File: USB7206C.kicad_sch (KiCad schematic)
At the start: 38 parts, among them J1 USB_SPI_(Opt), SW1 RESET_HUB, U1 USB7206C/KDX, U2 MIC803-29D4VM3-TR, Y1 25MHz

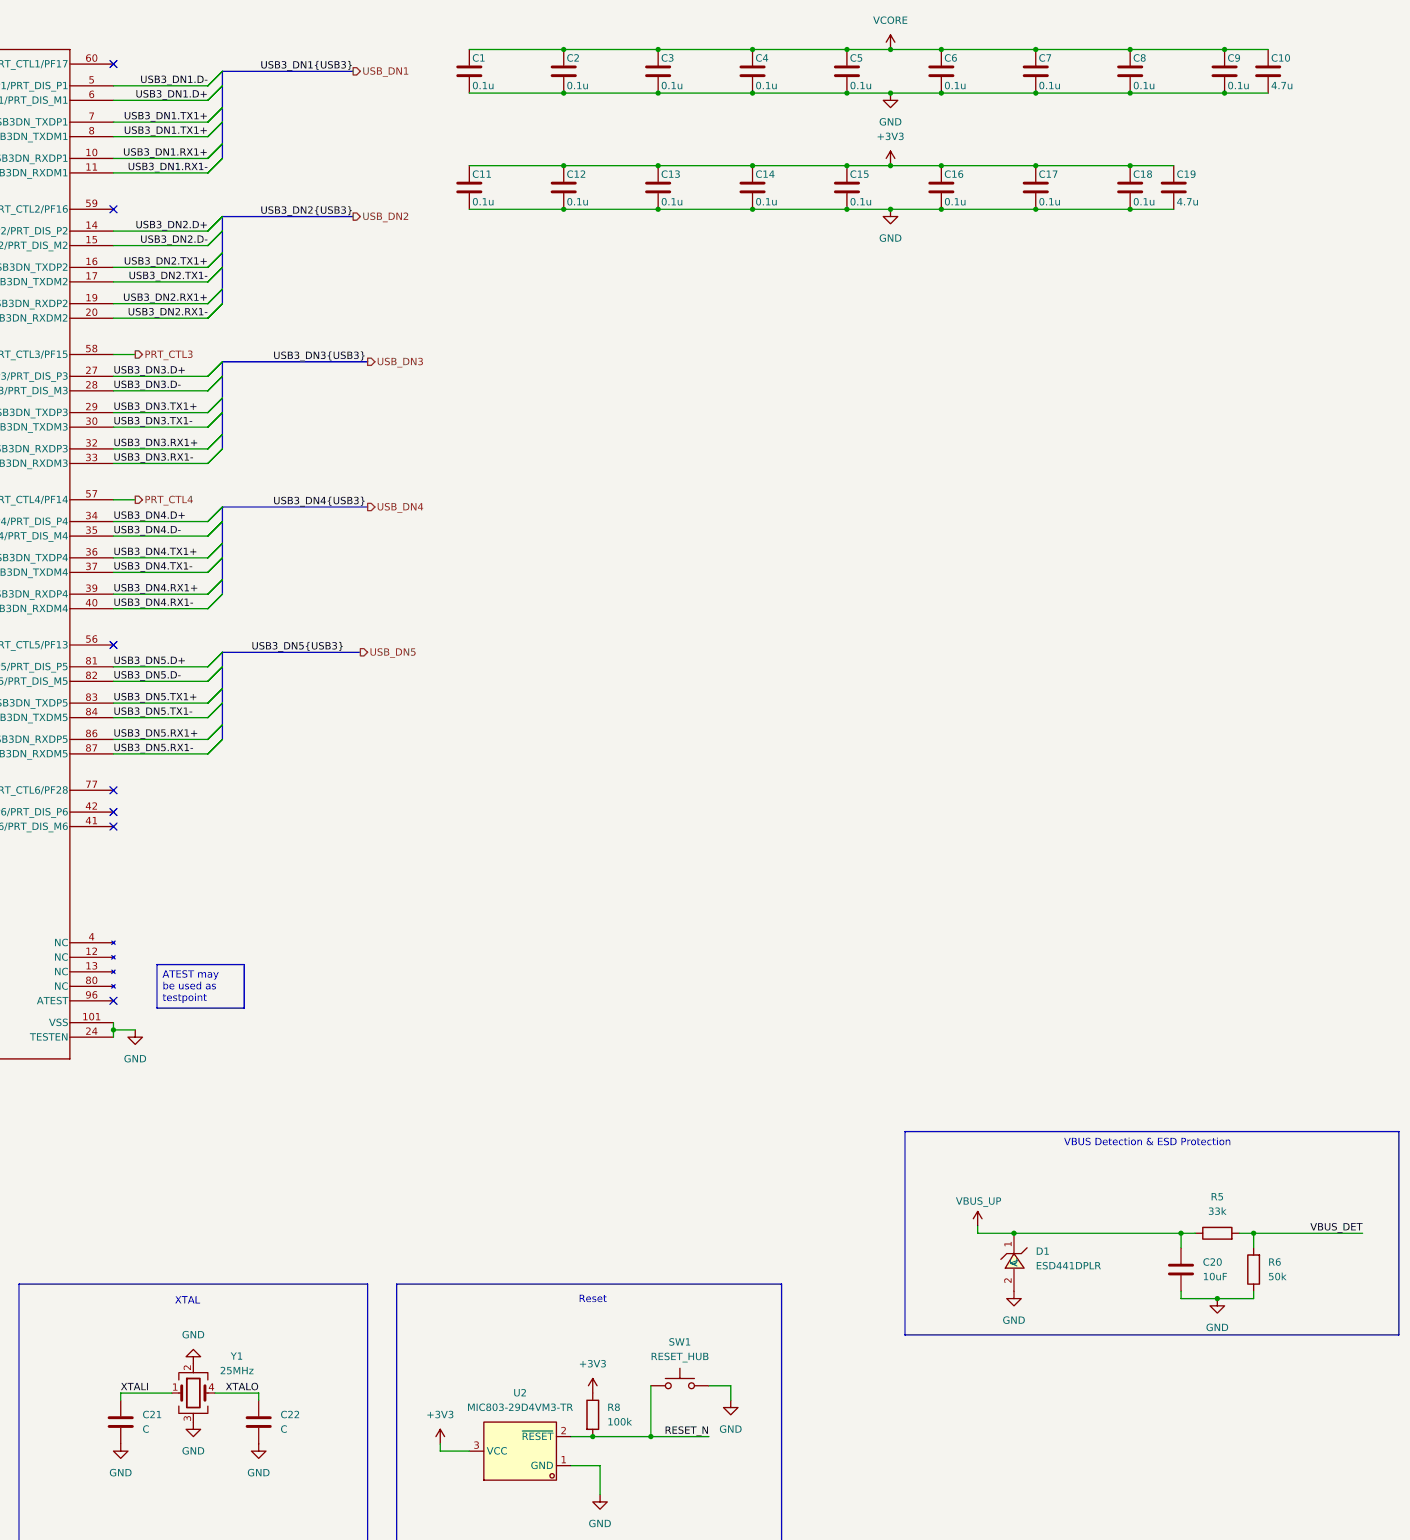
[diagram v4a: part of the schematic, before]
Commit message: Added lcsc part number for most of components, fixes for better routing
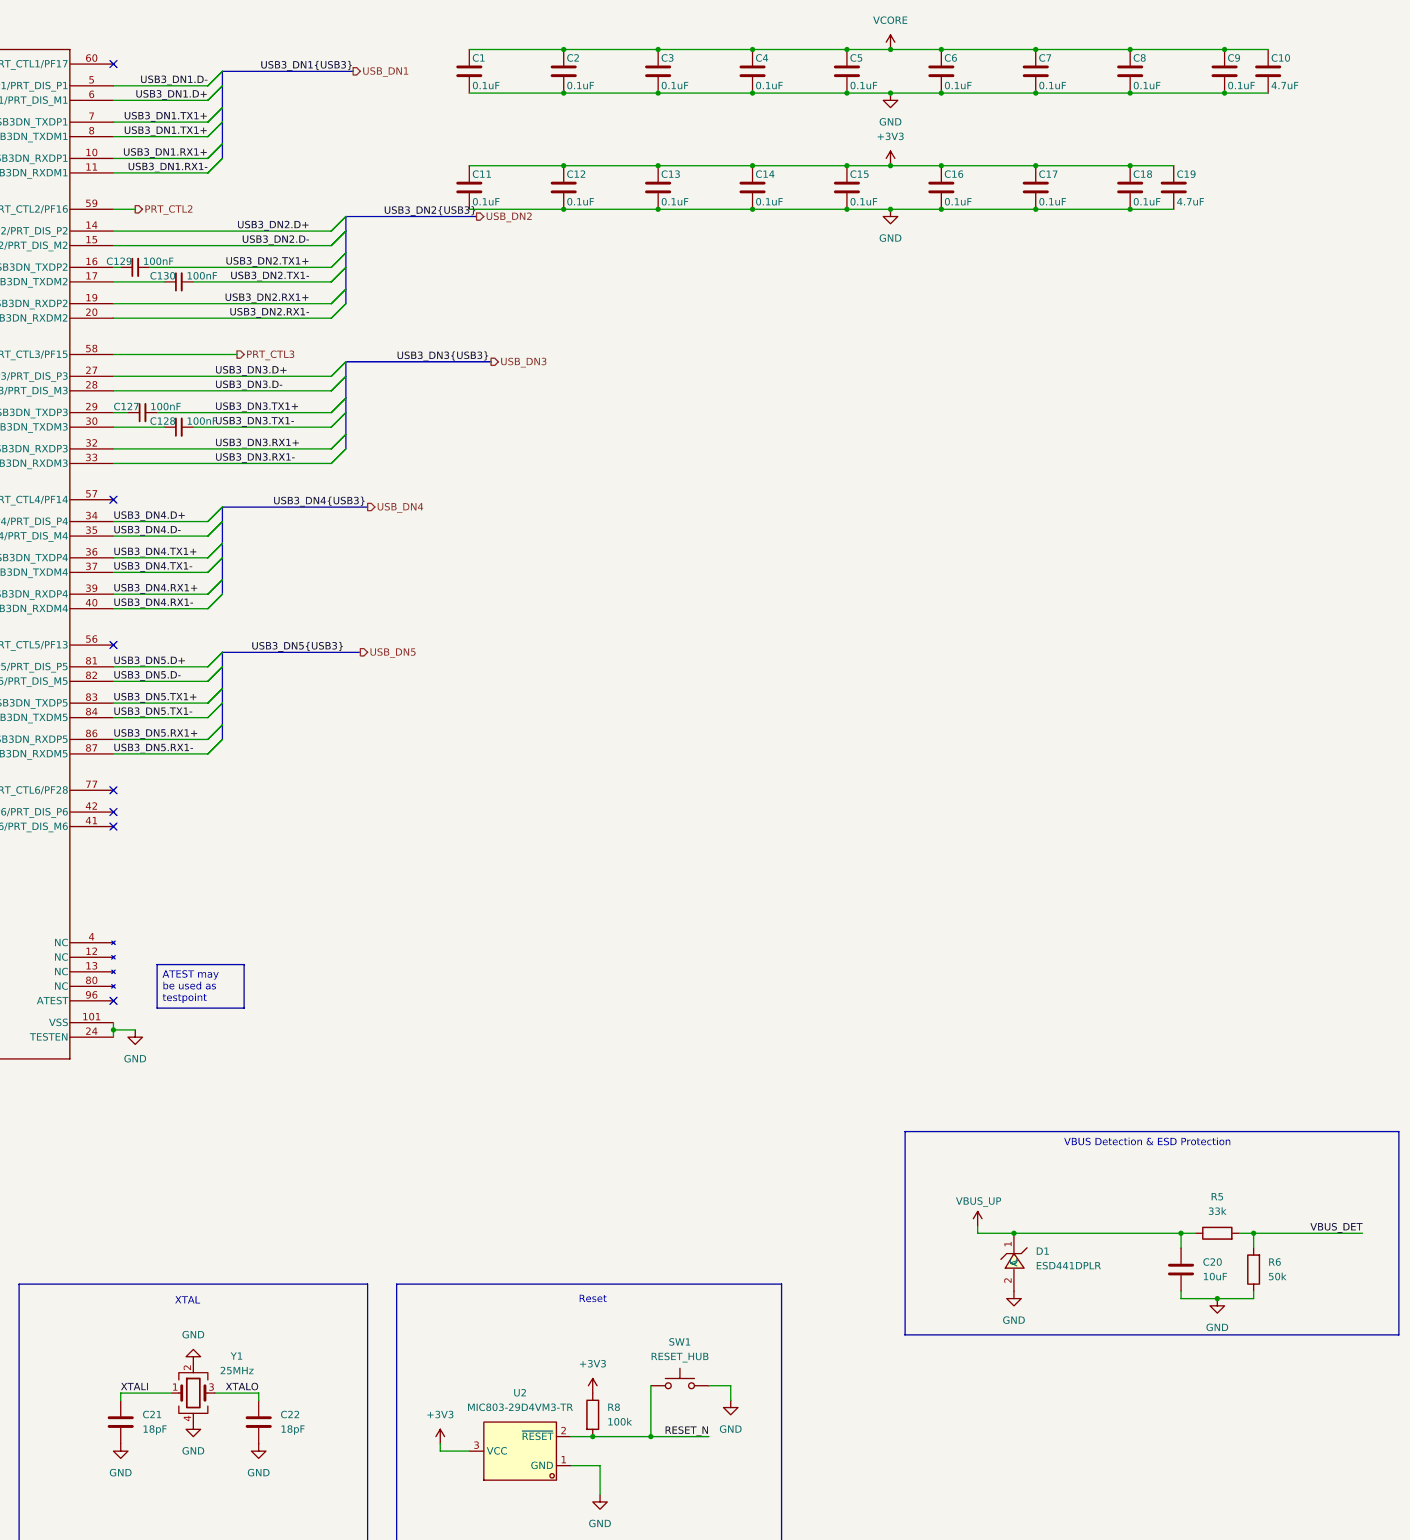
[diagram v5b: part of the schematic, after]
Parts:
- added C127, C128, C129, C130: 100nF, Capacitor_SMD:C_0402_1005Metric, symbol Device:C_Small
- C1, C11, C12, C13, C14, C15, C16, C17, C18, C2, C3, C4, C5, C6, C7, C8, C9: value 0.1u -> 0.1uF; LCSC Part (none) -> C5182432
- C10, C19: value 4.7u -> 4.7uF; footprint Capacitor_SMD:C_0402_1005Metric -> Capacitor_SMD:C_0805_2012Metric; LCSC Part (none) -> C6119944
- C20: footprint Capacitor_SMD:C_0402_1005Metric -> Capacitor_SMD:C_0805_2012Metric; LCSC Part (none) -> C3039694
- C21, C22: value C -> 18pF; LCSC Part (none) -> C33149
- Y1: footprint Crystal:Crystal_SMD_0603-4Pin_6.0x3.5mm -> Crystal:Crystal_SMD_3225-4Pin_3.2x2.5mm; LCSC Part (none) -> C179643
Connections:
- net GND: now also Y1.4; no longer Y1.3
- net USB3_DN2.TX1+: now also C129.2; no longer U1.16 (USB3DN_TXDP2)
- net USB3_DN2.TX1-: now also C130.2; no longer U1.17 (USB3DN_TXDM2)
- net USB3_DN3.TX1+: now also C127.2; no longer U1.29 (USB3DN_TXDP3)
- net USB3_DN3.TX1-: now also C128.2; no longer U1.30 (USB3DN_TXDM3)
- net XTALO: now also Y1.3; no longer Y1.4
- net PRT_CTL2: now reaches U1.59 (PRT_CTL2/PF16)
- net PRT_CTL4: no longer names the net of U1.57 (PRT_CTL4/PF14)
- new net: C130.1, U1.17 (USB3DN_TXDM2)
- new net: C127.1, U1.29 (USB3DN_TXDP3)
- new net: C128.1, U1.30 (USB3DN_TXDM3)
- new net: C129.1, U1.16 (USB3DN_TXDP2)

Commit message: Added lcsc part number for most of resistors
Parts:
- R1: LCSC Part (none) -> C102781
- R10, R9: LCSC Part (none) -> C25764
- R2, R3, R4, R7: LCSC Part (none) -> C25744
- R5: LCSC Part (none) -> C25779
- R6: LCSC Part (none) -> C166559
- R8: LCSC Part (none) -> C25741
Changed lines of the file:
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@@
 			)
 		)
+		(property "LCSC Part" "C25779 "
+			(at 365.76 227.33 90)
+			(effects
+				(font
+					(size 1.27 1.27)
+				)
+				(hide yes)
+			)
+		)
 		(pin "1"
 		)
@@
 			)
 		)
+		(property "LCSC Part" "C25741 "
+			(at 256.54 259.08 0)
+			(effects
+				(font
+					(size 1.27 1.27)
+				)
+				(hide yes)
+			)
+		)
 		(pin "2"
 		)
@@
 			)
 		)
+		(property "LCSC Part" "C25744"
+			(at 52.07 59.69 90)
+			(effects
+				(font
+					(size 1.27 1.27)
+				)
+				(hide yes)
+			)
+		)
 		(pin "1"
 		)
@@
 			)
 		)
+		(property "LCSC Part" "C25744"
+			(at 50.8 259.08 90)
+			(effects
+				(font
+					(size 1.27 1.27)
+				)
+				(hide yes)
+			)
+		)
 		(pin "2"
 		)
@@
 			)
 		)
+		(property "LCSC Part" "C25764 "
+			(at 50.8 264.16 90)
+			(effects
+				(font
+					(size 1.27 1.27)
+				)
+				(hide yes)
+			)
+		)
 		(pin "2"
 		)
@@
 			)
 		)
+		(property "LCSC Part" "C102781 "
+			(at 31.75 50.8 90)
+			(effects
+				(font
+					(size 1.27 1.27)
+				)
+				(hide yes)
+			)
+		)
 		(pin "1"
 		)
@@
 			)
 		)
+		(property "LCSC Part" "C25764 "
+			(at 50.8 261.62 90)
+			(effects
+				(font
+					(size 1.27 1.27)
+				)
+				(hide yes)
+			)
+		)
 		(pin "2"
 		)
@@
 			)
 		)
+		(property "LCSC Part" "C25744"
+			(at 52.07 54.61 90)
+			(effects
+				(font
+					(size 1.27 1.27)
+				)
+				(hide yes)
+			)
+		)
 		(pin "1"
 		)
@@
 			)
 		)
+		(property "LCSC Part" "C25744"
+			(at 52.07 57.15 90)
+			(effects
+				(font
+					(size 1.27 1.27)
+				)
+				(hide yes)
+			)
+		)
 		(pin "1"
 		)
@@
 			(at 372.11 233.68 0)
 			(effects
+				(font
+					(size 1.27 1.27)
+				)
+				(hide yes)
+			)
+		)
+		(property "LCSC Part" "C166559"
+			(at 372.11 233.68 0)
+			(effects

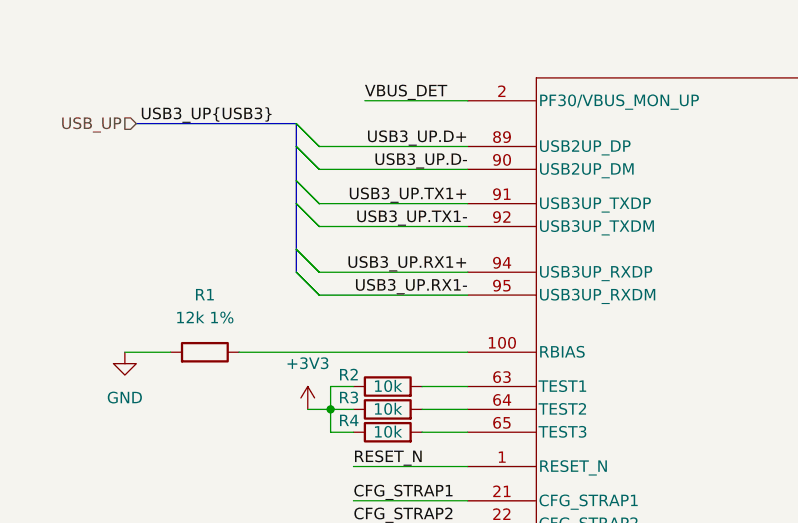
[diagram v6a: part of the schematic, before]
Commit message: minor schematic fixes, footprints changes, layout improvements
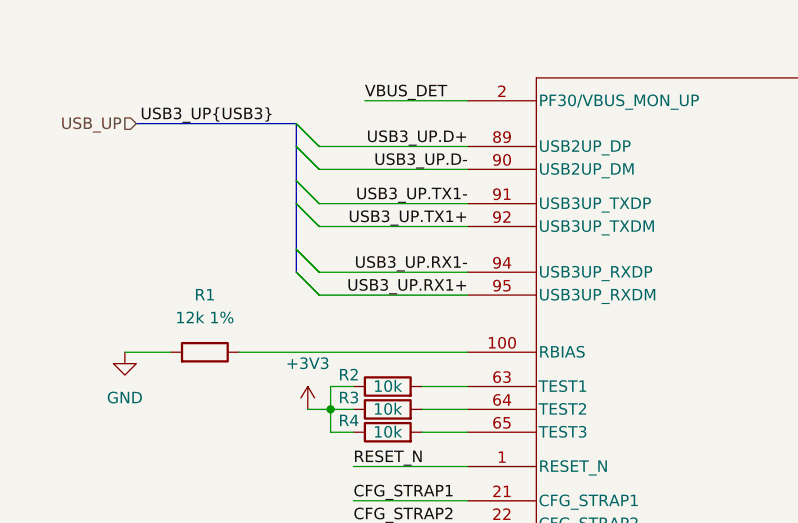
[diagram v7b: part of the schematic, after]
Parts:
- SW1: footprint Button_Switch_SMD:SW_Push_1P1T_XKB_TS-1187A -> EasyEDA:ultra_small_switch_1.6x3.0mm
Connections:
- net USB3_UP.RX1+: now also U1.95 (USB3UP_RXDM); no longer U1.94 (USB3UP_RXDP)
- net USB3_UP.RX1-: now also U1.94 (USB3UP_RXDP); no longer U1.95 (USB3UP_RXDM)
- net USB3_UP.TX1+: now also U1.92 (USB3UP_TXDM); no longer U1.91 (USB3UP_TXDP)
- net USB3_UP.TX1-: now also U1.91 (USB3UP_TXDP); no longer U1.92 (USB3UP_TXDM)
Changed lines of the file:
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@@
 		)
 	)
+	(wire
+		(pts
+			(xy 44.45 44.45) (xy 60.96 44.45)
+		)
+		(stroke
+			(width 0)
+			(type default)
+		)
+	)
 	(bus
 		(pts
@@
 	(wire
 		(pts
-			(xy 60.96 44.45) (xy 44.45 44.45)
-		)
-		(stroke
-			(width 0)
-			(type default)
-		)
-	)
-	(wire
-		(pts
 			(xy 186.69 60.96) (xy 210.82 60.96)
 		)
@@
 		)
 	)
-	(label "USB3_DN1.RX1+"
-		(at 189.23 39.37 180)
+	(label "USB3_UP.TX1-"
+		(at 60.96 34.29 180)
 		(effects
 			(font
@@
 		)
 	)
-	(label "USB3_UP.TX1+"
-		(at 60.96 34.29 180)
+	(label "USB3_DN1.RX1+"
+		(at 189.23 39.37 180)
 		(effects
 			(font
@@
 		)
 	)
+	(label "USB3_UP.TX1+"
+		(at 60.96 36.83 180)
+		(effects
+			(font
+				(size 1.27 1.27)
+			)
+			(justify right bottom)
+		)
+	)
 	(label "USB3_UP.D+"
 		(at 60.96 27.94 180)
@@
 		)
 	)
+	(label "USB3_UP.RX1-"
+		(at 60.96 41.91 180)
+		(effects
+			(font
+				(size 1.27 1.27)
+			)
+			(justify right bottom)
+		)
+	)
 	(label "USB3_DN2{USB3}"
 		(at 236.22 49.53 180)
@@
 		)
 	)
-	(label "USB3_UP.RX1-"
-		(at 60.96 44.45 180)
-		(effects
-			(font
-				(size 1.27 1.27)
-			)
-			(justify right bottom)
-		)
-	)
 	(label "USB3_DN1.D+"
 		(at 189.23 29.21 180)
@@
 		)
 	)
-	(label "USB3_UP.RX1+"
-		(at 60.96 41.91 180)
-		(effects
-			(font
-				(size 1.27 1.27)
-			)
-			(justify right bottom)
-		)
-	)
 	(label "USB3_DN1.D-"
 		(at 189.23 26.67 180)
@@
 		)
 	)
-	(label "USB3_UP.TX1-"
-		(at 60.96 36.83 180)
+	(label "USB3_DN3.D-"
+		(at 190.5 80.01 0)
 		(effects
 			(font
 				(size 1.27 1.27)
 			)
-			(justify right bottom)
+			(justify left bottom)
 		)
 	)
-	(label "USB3_DN3.D-"
-		(at 190.5 80.01 0)
+	(label "USB3_UP.RX1+"
+		(at 60.96 44.45 180)
 		(effects
 			(font
 				(size 1.27 1.27)
 			)
-			(justify left bottom)
+			(justify right bottom)
 		)
 	)
@@
 			)
 		)
-		(property "Footprint" "Button_Switch_SMD:SW_Push_1P1T_XKB_TS-1187A"
+		(property "Footprint" "EasyEDA:ultra_small_switch_1.6x3.0mm"
 			(at 271.78 248.92 0)
 			(effects

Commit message: comments to schematic added, changed a few components
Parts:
- SW1: LCSC Part (none) -> C913788
- U1: Mouser Part No  (none) -> 579-USB7206C/KDX
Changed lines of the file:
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@@
+			)
+		)
+		(property "LCSC Part" "C913788 "
+			(at 271.78 254 0)
+			(effects
+				(font
+					(size 1.27 1.27)
+				)
+				(hide yes)
 			)
 		)
@@
 			(at 60.96 25.4 0)
 			(effects
+				(font
+					(size 1.27 1.27)
+				)
+				(hide yes)
+			)
+		)
+		(property "Mouser Part No " "579-USB7206C/KDX "
+			(at 60.96 25.4 0)
+			(effects
